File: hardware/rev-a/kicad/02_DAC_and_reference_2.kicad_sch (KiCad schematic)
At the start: 4 parts

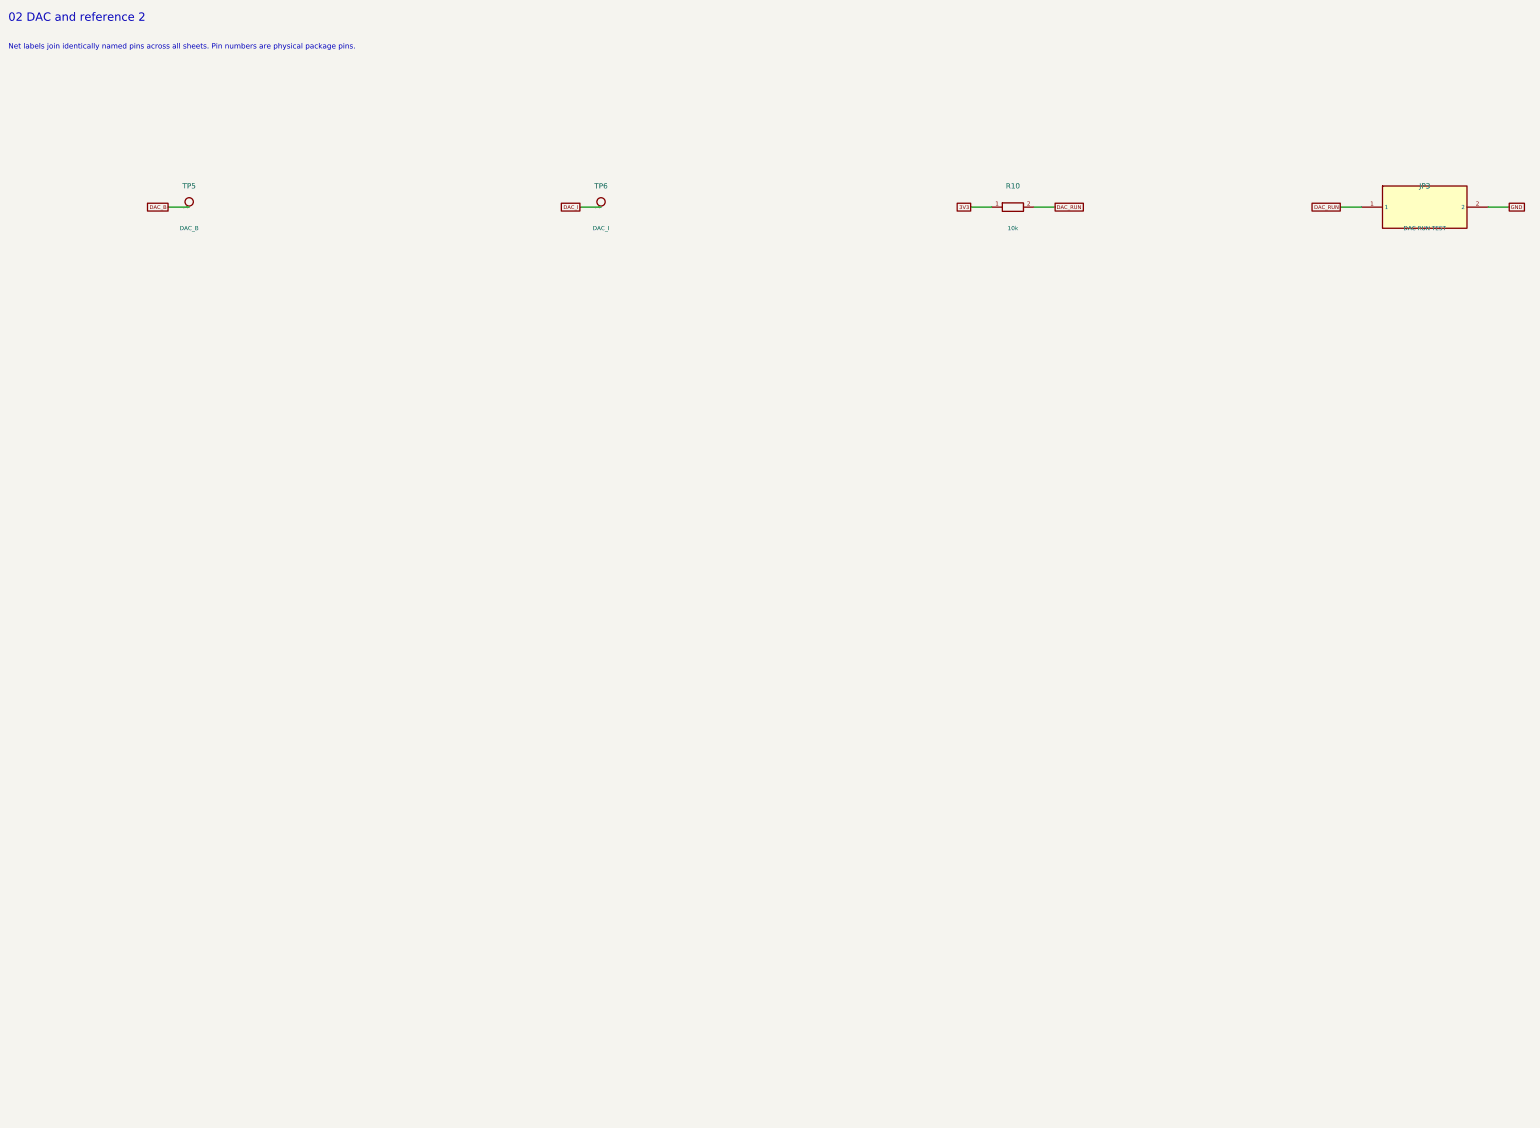
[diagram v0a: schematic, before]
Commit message: Redraw Rev.A schematics with functional blocks and explicit wiring
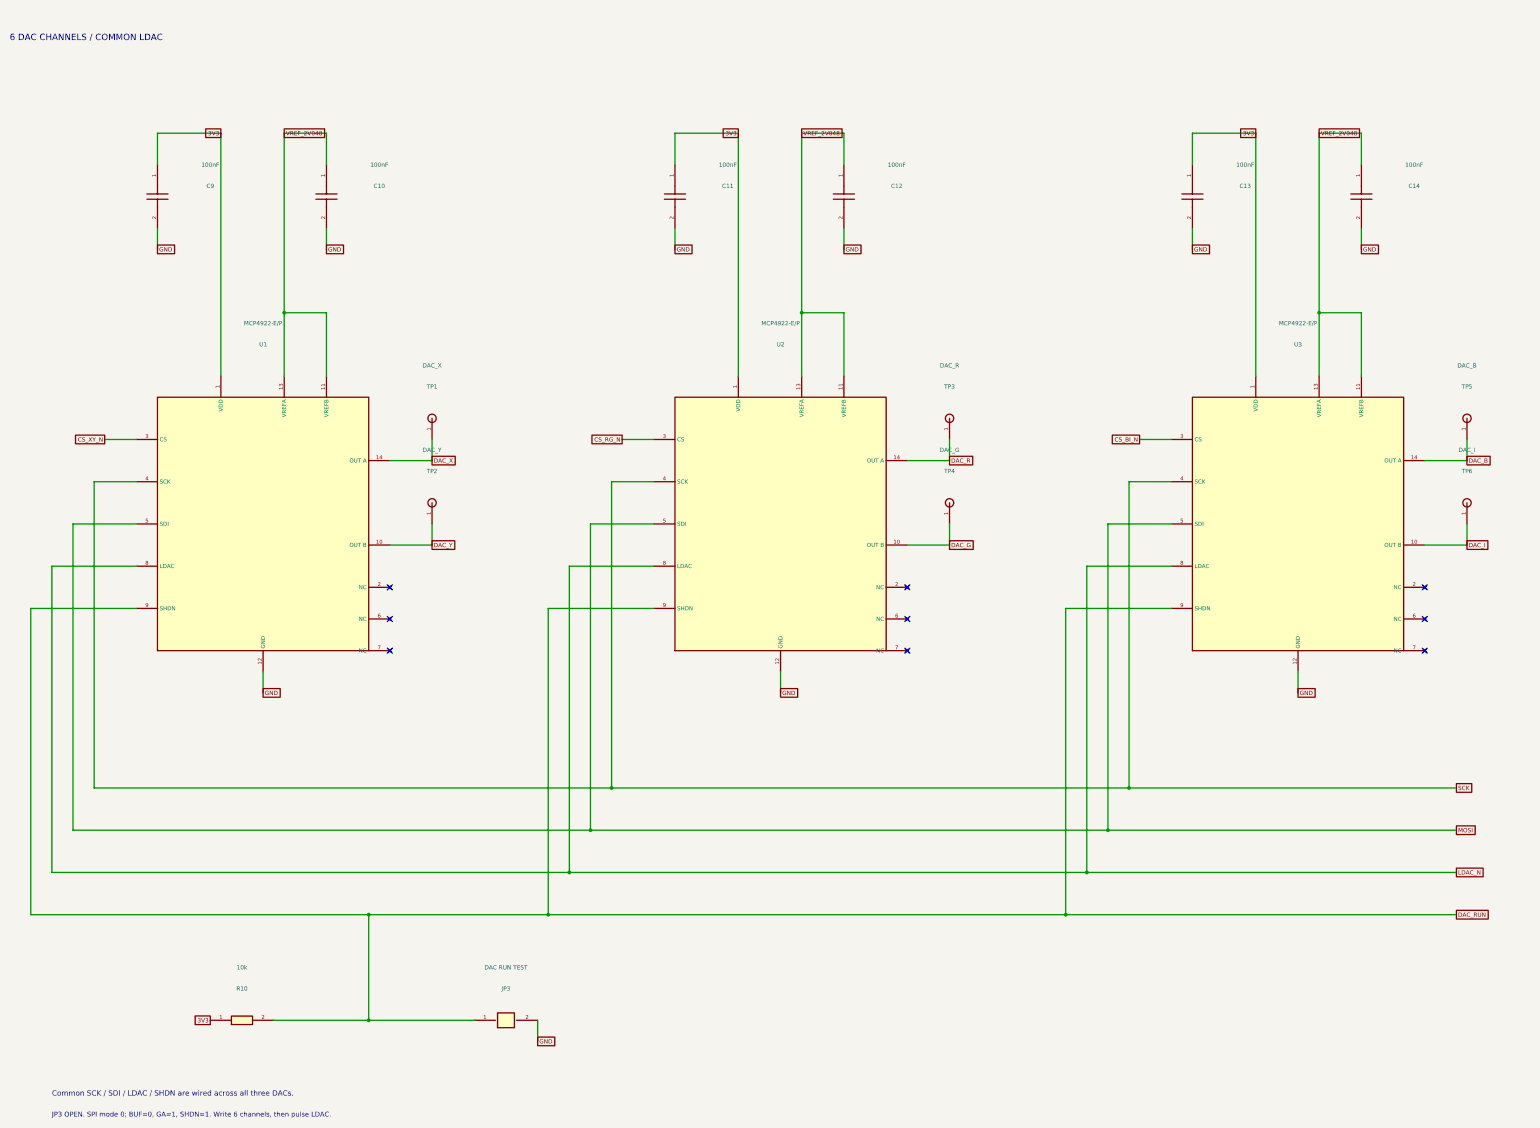
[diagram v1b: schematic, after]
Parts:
- added C10, C11, C12, C13, C14, C9: 100nF, RevA:C_Disc_D5.0mm_W2.5mm_P5.00mm, symbol RevA:C
- added TP1: DAC_X, RevA:TestPoint_THTPad_D2.0mm_Drill1.0mm, symbol RevA:TP
- added TP2: DAC_Y, RevA:TestPoint_THTPad_D2.0mm_Drill1.0mm, symbol RevA:TP
- added TP3: DAC_R, RevA:TestPoint_THTPad_D2.0mm_Drill1.0mm, symbol RevA:TP
- added TP4: DAC_G, RevA:TestPoint_THTPad_D2.0mm_Drill1.0mm, symbol RevA:TP
- added U1: MCP4922-E/P, RevA:DIP-14_W7.62mm, symbol RevA:Part_U1
- added U2: MCP4922-E/P, RevA:DIP-14_W7.62mm, symbol RevA:Part_U2
- added U3: MCP4922-E/P, RevA:DIP-14_W7.62mm, symbol RevA:Part_U3
- JP3: symbol RevA:Conn_JP3 -> RevA:Link
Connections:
- net 3V3: now also C11.1, C13.1, C9.1, U1.1 (VDD), U2.1 (VDD), U3.1 (VDD)
- net DAC_B: now also U3.14 (OUT A)
- net DAC_I: now also U3.10 (OUT B)
- net DAC_RUN: now also U1.9 (SHDN), U2.9 (SHDN), U3.9 (SHDN)
- net GND: now also C10.2, C11.2, C12.2, C13.2, C14.2, C9.2, U1.12 (GND), U2.12 (GND), U3.12 (GND)
- new net CS_BI_N: U3.3 (CS)
- new net CS_RG_N: U2.3 (CS)
- new net CS_XY_N: U1.3 (CS)
- new net DAC_G: TP4.1, U2.10 (OUT B)
- new net DAC_R: TP3.1, U2.14 (OUT A)
- new net DAC_X: TP1.1, U1.14 (OUT A)
- new net DAC_Y: TP2.1, U1.10 (OUT B)
- new net LDAC_N: U1.8 (LDAC), U2.8 (LDAC), U3.8 (LDAC)
- new net MOSI: U1.5 (SDI), U2.5 (SDI), U3.5 (SDI)
- new net SCK: U1.4 (SCK), U2.4 (SCK), U3.4 (SCK)
- new net VREF_2V048: C10.1, C12.1, C14.1, U1.11 (VREFB), U1.13 (VREFA), U2.11 (VREFB), U2.13 (VREFA), U3.11 (VREFB), U3.13 (VREFA)
- no-connect marks 0 -> 9
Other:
- note added: "6 DAC CHANNELS / COMMON LDAC"
- note added: "Common SCK / SDI / LDAC / SHDN are wired across all three DACs."
- note added: "JP3 OPEN. SPI mode 0; BUF=0, GA=1, SHDN=1. Write 6 channels, then pulse LDAC."
- note removed: "02 DAC and reference 2"
- note removed: "Net labels join identically named pins across all sheets. Pin numbers are physical package pins."
- company: CoreS3 ILDA evaluation -> (none)
- title: 02_DAC_and_reference_2 -> 04 / Six-channel DAC bank
